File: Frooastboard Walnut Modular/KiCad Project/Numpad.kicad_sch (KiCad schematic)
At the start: 68 parts, among them J19 Conn_01x15_Male, J20 Conn_01x06_Male, J21 Conn_01x13_Male, M1 Frooastboard_MM2040

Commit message: before nrf52810
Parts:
- added D? (x4): RGB_LED_6_Pin, Frooastboard Footprints:Everlight 99-235, symbol Frooastboard Symbols:RGB_LED_6_Pin
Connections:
- net SW6 is gone; now on net CS13: D76.5 (B-), D77.5 (B-), D78.5 (B-), D79.5 (B-), J20.3 (Pin_3), M1.6 (SW6)
- net CS13: now also D?.2 (G+), D?.4 (R+), D?.6 (B+)
- net CS14: now also D?.2 (G+), D?.4 (R+), D?.6 (B+)
- net CS15: now also D?.2 (G+), D?.4 (R+), D?.6 (B+)
- net CS16: now also D?.2 (G+), D?.4 (R+), D?.6 (B+)
- net SW4: now also D?.1 (G-), D?.1 (G-), D?.1 (G-), D?.1 (G-)
- net SW5: now also D?.3 (R-), D?.3 (R-), D?.3 (R-), D?.3 (R-)
- new net: D?.5 (B-), D?.5 (B-), D?.5 (B-), D?.5 (B-)

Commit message: some new stuff
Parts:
- removed D52, D58, D64, D68, D70: D_Small, symbol Device:D_Small
- removed MX22, MX27, MX33, MX36, MX38: MX-NoLED, symbol MX_Alps_Hybrid:MX-NoLED
- added D58: Num Lock Indicator, LED_SMD:LED_0805_2012Metric, symbol Device:LED
- C40: footprint (none) -> Capacitor_SMD:C_0805_2012Metric
- D47, D48, D49, D50, D51, D54, D55, D56, D57, D59, D60, D61, D62, D63, D66, D67, D69: footprint (none) -> Diode_SMD:D_0805_2012Metric
- J19: footprint (none) -> Frooastboard Footprints:PinHeader_1x15_P1.27mm_Vertical
- J20: footprint (none) -> Frooastboard Footprints:PinHeader_1x06_P1.27mm_Vertical
- J21: footprint (none) -> Frooastboard Footprints:PinHeader_1x13_P1.27mm_Vertical
- MX17: value MX-NoLED -> Num Lock
- MX18: value MX-NoLED -> Num 7
- MX19: value MX-NoLED -> Num 4
- MX20: value MX-NoLED -> Num 1
- MX21: value MX-NoLED -> Num 0
- MX23: value MX-NoLED -> Multiply
- MX24: value MX-NoLED -> Num 9
- MX25: value MX-NoLED -> Num 6
- MX26: value MX-NoLED -> Num 3
- MX28: value MX-NoLED -> Divide
- MX29: value MX-NoLED -> Num 8
- MX30: value MX-NoLED -> Num 5
- MX31: value MX-NoLED -> Num 2
- MX32: value MX-NoLED -> Comma
- MX34: value MX-NoLED -> Minus
- MX35: value MX-NoLED -> Plus
- MX37: value MX-NoLED -> Enter
- gave numbers to parts that had none: 4
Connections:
- net CS13: now also D58.1 (K)
- net CS2: now also D58.2 (A)
- no-connect marks 17 -> 19

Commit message: asign pieces
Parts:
- MX17: footprint (none) -> MX_Only:MXOnly-1U
- MX18, MX19, MX20, MX23, MX24, MX25, MX26, MX28, MX29, MX30, MX31, MX32, MX34: footprint (none) -> MX_Only:MXOnly-1U-NoLED
- MX21: footprint (none) -> MX_Only:MXOnly-2U-NoLED
- MX35, MX37: footprint (none) -> MX_Only:MXOnly-2U-VerticalStabilizers-NoLED
- R31: footprint (none) -> Resistor_SMD:R_0805_2012Metric
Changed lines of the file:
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@@
       (effects (font (size 0.508 0.508)))
     )
-    (property "Footprint" "" (id 2) (at 127.635 227.965 0)
+    (property "Footprint" "MX_Only:MXOnly-1U-NoLED" (id 2) (at 127.635 227.965 0)
       (effects (font (size 1.524 1.524)) hide)
     )
@@
       (effects (font (size 0.508 0.508)))
     )
-    (property "Footprint" "" (id 2) (at 108.585 192.405 0)
+    (property "Footprint" "MX_Only:MXOnly-1U-NoLED" (id 2) (at 108.585 192.405 0)
       (effects (font (size 1.524 1.524)) hide)
     )
@@
       (effects (font (size 0.508 0.508)))
     )
-    (property "Footprint" "" (id 2) (at 108.585 227.965 0)
+    (property "Footprint" "MX_Only:MXOnly-2U-NoLED" (id 2) (at 108.585 227.965 0)
       (effects (font (size 1.524 1.524)) hide)
     )
@@
       (effects (font (size 0.508 0.508)))
     )
-    (property "Footprint" "" (id 2) (at 136.525 159.385 0)
+    (property "Footprint" "MX_Only:MXOnly-1U-NoLED" (id 2) (at 136.525 159.385 0)
       (effects (font (size 1.524 1.524)) hide)
     )
@@
       (effects (font (size 0.508 0.508)))
     )
-    (property "Footprint" "" (id 2) (at 108.585 210.185 0)
+    (property "Footprint" "MX_Only:MXOnly-1U-NoLED" (id 2) (at 108.585 210.185 0)
       (effects (font (size 1.524 1.524)) hide)
     )
@@
       (effects (font (size 0.508 0.508)))
     )
-    (property "Footprint" "" (id 2) (at 127.635 192.405 0)
+    (property "Footprint" "MX_Only:MXOnly-1U-NoLED" (id 2) (at 127.635 192.405 0)
       (effects (font (size 1.524 1.524)) hide)
     )
@@
       (effects (font (size 0.508 0.508)))
     )
-    (property "Footprint" "" (id 2) (at 117.475 177.165 0)
+    (property "Footprint" "MX_Only:MXOnly-1U-NoLED" (id 2) (at 117.475 177.165 0)
       (effects (font (size 1.524 1.524)) hide)
     )
@@
       (effects (font (size 0.508 0.508)))
     )
-    (property "Footprint" "" (id 2) (at 117.475 194.945 0)
+    (property "Footprint" "MX_Only:MXOnly-1U-NoLED" (id 2) (at 117.475 194.945 0)
       (effects (font (size 1.524 1.524)) hide)
     )
@@
       (effects (font (size 0.508 0.508)))
     )
-    (property "Footprint" "" (id 2) (at 108.585 156.845 0)
+    (property "Footprint" "MX_Only:MXOnly-1U" (id 2) (at 108.585 156.845 0)
       (effects (font (size 1.524 1.524)) hide)
     )
@@
       (effects (font (size 0.508 0.508)))
     )
-    (property "Footprint" "" (id 2) (at 117.475 159.385 0)
+    (property "Footprint" "MX_Only:MXOnly-1U-NoLED" (id 2) (at 117.475 159.385 0)
       (effects (font (size 1.524 1.524)) hide)
     )
@@
       (effects (font (size 0.508 0.508)))
     )
-    (property "Footprint" "" (id 2) (at 108.585 174.625 0)
+    (property "Footprint" "MX_Only:MXOnly-1U-NoLED" (id 2) (at 108.585 174.625 0)
       (effects (font (size 1.524 1.524)) hide)
     )
@@
       (effects (font (size 0.508 0.508)))
     )
-    (property "Footprint" "" (id 2) (at 136.525 212.725 0)
+    (property "Footprint" "MX_Only:MXOnly-2U-VerticalStabilizers-NoLED" (id 2) (at 136.525 212.725 0)
       (effects (font (size 1.524 1.524)) hide)
     )
@@
       (effects (font (size 0.508 0.508)))
     )
-    (property "Footprint" "" (id 2) (at 127.635 174.625 0)
+    (property "Footprint" "MX_Only:MXOnly-1U-NoLED" (id 2) (at 127.635 174.625 0)
       (effects (font (size 1.524 1.524)) hide)
     )
@@
       (effects (font (size 0.508 0.508)))
     )
-    (property "Footprint" "" (id 2) (at 127.635 156.845 0)
+    (property "Footprint" "MX_Only:MXOnly-1U-NoLED" (id 2) (at 127.635 156.845 0)
       (effects (font (size 1.524 1.524)) hide)
     )
@@
       (effects (font (size 0.508 0.508)))
     )
-    (property "Footprint" "" (id 2) (at 136.525 177.165 0)
+    (property "Footprint" "MX_Only:MXOnly-2U-VerticalStabilizers-NoLED" (id 2) (at 136.525 177.165 0)
       (effects (font (size 1.524 1.524)) hide)
     )
@@
       (effects (font (size 1.27 1.27)) (justify left))
     )
-    (property "Footprint" "" (id 2) (at 270.002 121.92 90)
+    (property "Footprint" "Resistor_SMD:R_0805_2012Metric" (id 2) (at 270.002 121.92 90)
       (effects (font (size 1.27 1.27)) hide)
     )
@@
       (effects (font (size 0.508 0.508)))
     )
-    (property "Footprint" "" (id 2) (at 127.635 210.185 0)
+    (property "Footprint" "MX_Only:MXOnly-1U-NoLED" (id 2) (at 127.635 210.185 0)
       (effects (font (size 1.524 1.524)) hide)
     )
@@
       (effects (font (size 0.508 0.508)))
     )
-    (property "Footprint" "" (id 2) (at 117.475 212.725 0)
-      (effects (font (size 1.524 1.524)) hide)
-    )
+    (property "Footprint" "MX_Only:MXOnly-1U-NoLED" (id 2) (at 117.475 212.725 0)
+      (effects (font (size 1.524 1.524)) hide)
+    )

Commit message: change some stuff maybe finally get started
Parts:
- J19: footprint Frooastboard Footprints:PinHeader_1x15_P1.27mm_Vertical -> Connector_PinHeader_1.27mm:PinHeader_1x15_P1.27mm_Vertical
- J20: footprint Frooastboard Footprints:PinHeader_1x06_P1.27mm_Vertical -> Connector_PinHeader_1.27mm:PinHeader_1x06_P1.27mm_Vertical
- J21: footprint Frooastboard Footprints:PinHeader_1x13_P1.27mm_Vertical -> Connector_PinHeader_1.27mm:PinHeader_1x13_P1.27mm_Vertical

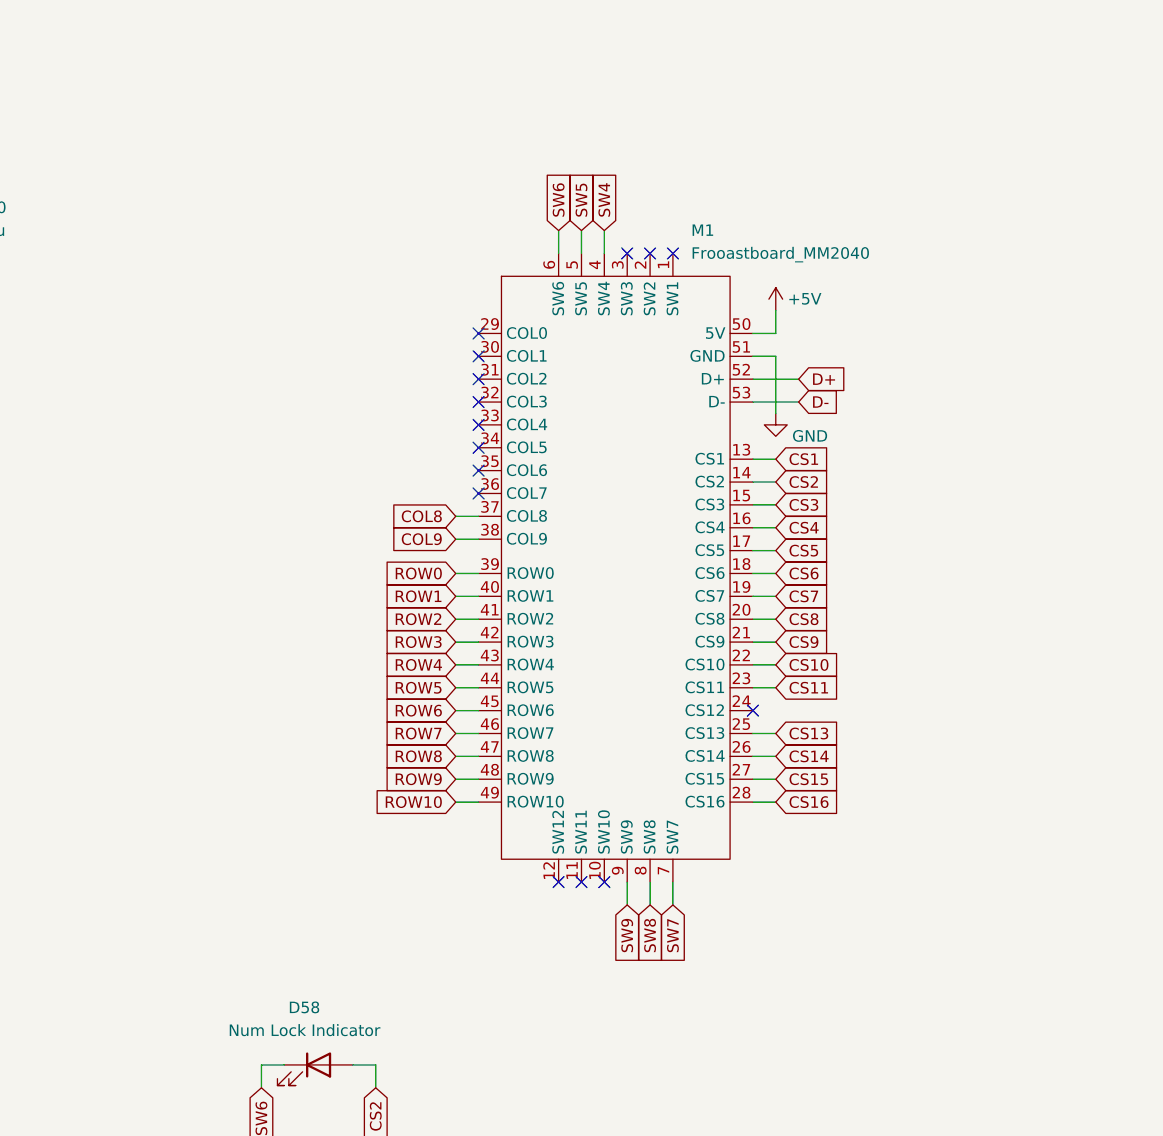
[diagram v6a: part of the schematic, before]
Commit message: import mm2040
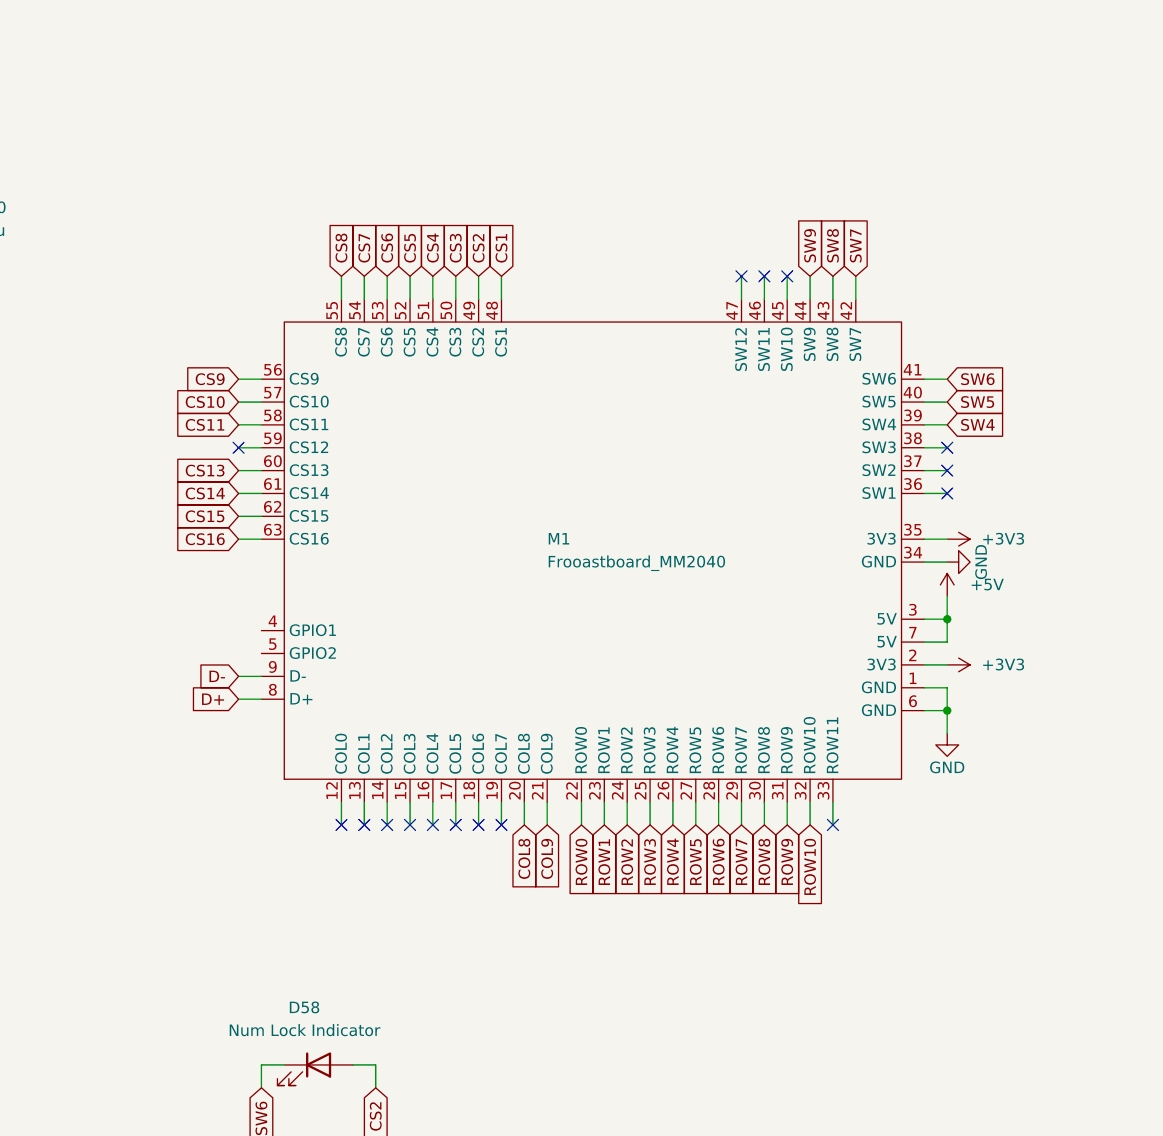
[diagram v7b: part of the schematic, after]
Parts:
- M1: footprint (none) -> Frooastboard Footprints:MM2040
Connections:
- net +5V: now also M1.3 (5V), M1.7 (5V); no longer M1.50 (5V)
- net COL8: now also M1.20 (COL8); no longer M1.37 (COL8)
- net COL9: now also M1.21 (COL9); no longer M1.38 (COL9)
- net CS1: now also M1.48 (CS1); no longer M1.13 (CS1)
- net CS10: now also M1.57 (CS10); no longer M1.22 (CS10)
- net CS11: now also M1.58 (CS11); no longer M1.23 (CS11)
- net CS13: now also M1.41 (SW6), M1.60 (CS13); no longer M1.25 (CS13), M1.6 (SW6)
- net CS14: now also M1.61 (CS14); no longer M1.26 (CS14)
- net CS15: now also M1.62 (CS15); no longer M1.27 (CS15)
- net CS16: now also M1.63 (CS16); no longer M1.28 (CS16)
- net CS2: now also M1.49 (CS2); no longer M1.14 (CS2)
- net CS3: now also M1.50 (CS3); no longer M1.15 (CS3)
- net CS4: now also M1.51 (CS4); no longer M1.16 (CS4)
- net CS5: now also M1.52 (CS5); no longer M1.17 (CS5)
- net CS6: now also M1.53 (CS6); no longer M1.18 (CS6)
- net CS7: now also M1.54 (CS7); no longer M1.19 (CS7)
- net CS8: now also M1.55 (CS8); no longer M1.20 (CS8)
- net CS9: now also M1.56 (CS9); no longer M1.21 (CS9)
- net D+: now also M1.8 (D+); no longer M1.52 (D+)
- net D-: now also M1.9 (D-); no longer M1.53 (D-)
- net GND: now also M1.1 (GND), M1.34 (GND), M1.6 (GND); no longer M1.51 (GND)
- net ROW0: now also M1.22 (ROW0); no longer M1.39 (ROW0)
- net ROW1: now also M1.23 (ROW1); no longer M1.40 (ROW1)
- net ROW10: now also M1.32 (ROW10); no longer M1.49 (ROW10)
- net ROW2: now also M1.24 (ROW2); no longer M1.41 (ROW2)
- net ROW3: now also M1.25 (ROW3); no longer M1.42 (ROW3)
- net ROW4: now also M1.26 (ROW4); no longer M1.43 (ROW4)
- net ROW5: now also M1.27 (ROW5); no longer M1.44 (ROW5)
- net ROW6: now also M1.28 (ROW6); no longer M1.45 (ROW6)
- net ROW7: now also M1.29 (ROW7); no longer M1.46 (ROW7)
- net ROW8: now also M1.30 (ROW8); no longer M1.47 (ROW8)
- net ROW9: now also M1.31 (ROW9); no longer M1.48 (ROW9)
- net SW4: now also M1.39 (SW4); no longer M1.4 (SW4)
- net SW5: now also M1.40 (SW5); no longer M1.5 (SW5)
- net SW7: now also M1.42 (SW7); no longer M1.7 (SW7)
- net SW8: now also M1.43 (SW8); no longer M1.8 (SW8)
- net SW9: now also M1.44 (SW9); no longer M1.9 (SW9)
- net +3V3: now reaches M1.2 (3V3)
- net +3V3: now also M1.35 (3V3)
- no-connect marks 19 -> 20

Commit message: some leds and stuff
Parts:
- MX21: footprint MX_Only:MXOnly-2U-NoLED -> MX_Only:MXOnly-2U-ReversedStabilizers-NoLED
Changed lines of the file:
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@@
       (effects (font (size 0.508 0.508)))
     )
-    (property "Footprint" "MX_Only:MXOnly-2U-NoLED" (at 108.585 227.965 0)
+    (property "Footprint" "MX_Only:MXOnly-2U-ReversedStabilizers-NoLED" (at 108.585 227.965 0)
       (effects (font (size 1.524 1.524)) hide)
     )
